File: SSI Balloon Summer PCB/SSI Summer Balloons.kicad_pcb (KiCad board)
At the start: 4 copper layers, 94.5 x 59 mm, 105 parts, among them J1 Battery connector, J2 Conn_01x02, J3 LoRa antenna, J4 APRS antenna, J5 Conn_01x05, J6 1040310811, J7 GPS antenna, J8 PT1000 Sensor, J9 Camera, Q2 DMG2305UX-7, SW2 SW_SPST, SW3 SW_SPST, U1 RFM95W-915S2, U10 MS5611-01BA03, U11 TPS63070RNMR, U12 TPS63070RNMR, U3 AP2112K-3.3TRG1, U4 ICM-42688-P, U5 DRA818V, U7 STM32F411CEUx, U8 MAX-M10S-00B, U9 MAX31865ATP_T, Y1 ABM8W-12.0000MHZ-8-K1Z-T3

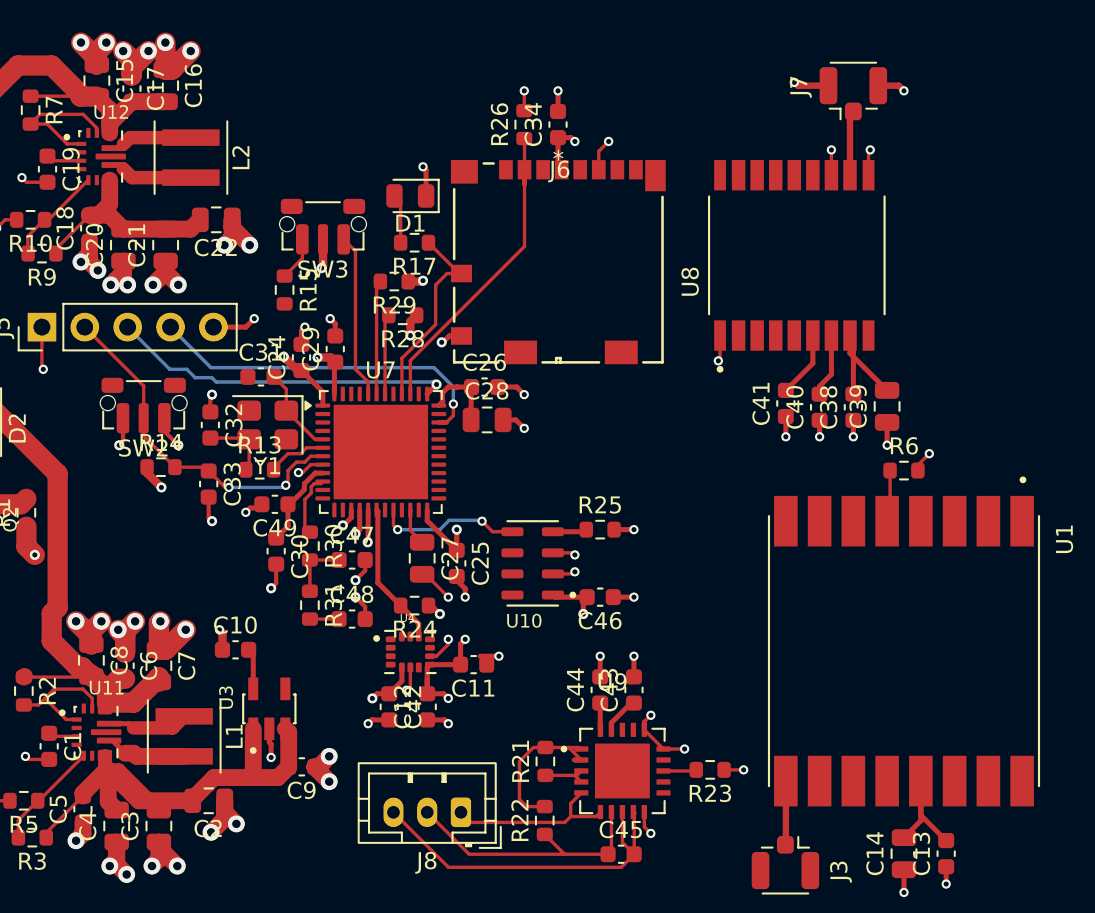
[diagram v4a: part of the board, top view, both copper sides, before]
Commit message: Routed most of SPI
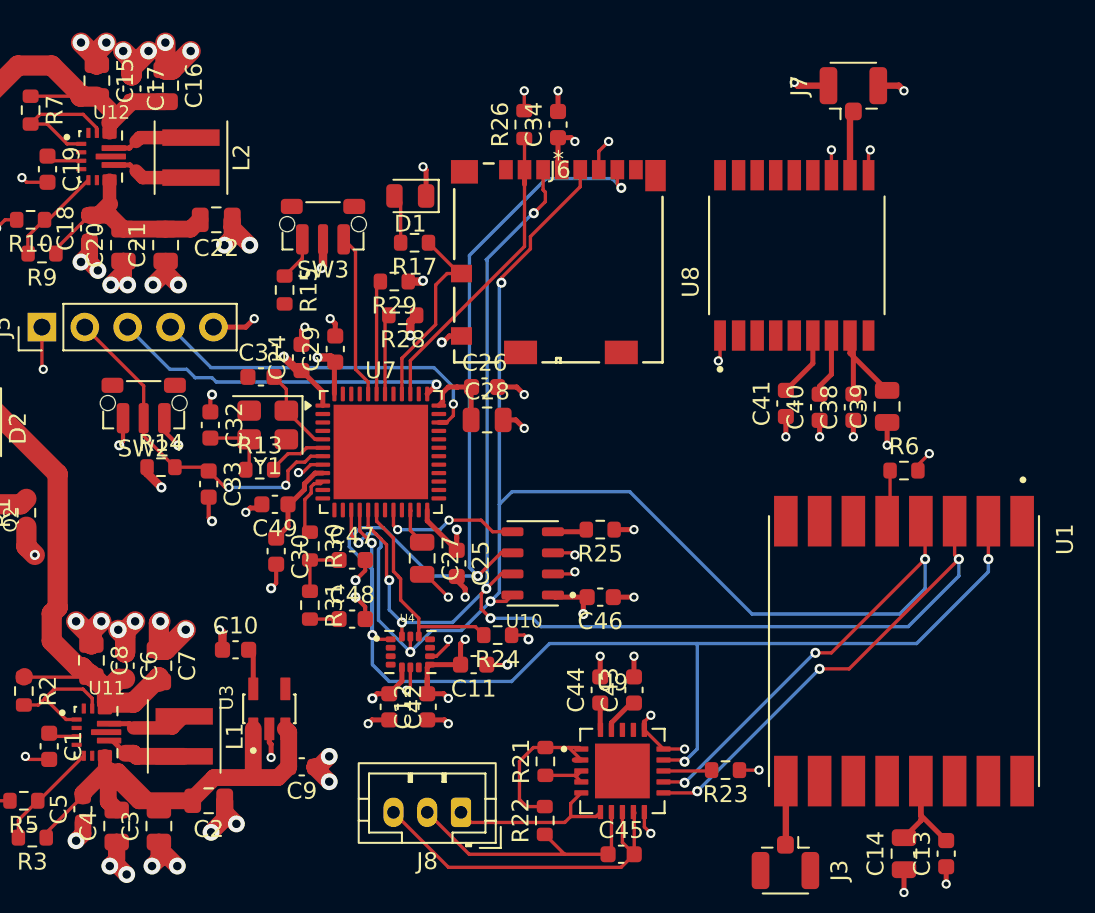
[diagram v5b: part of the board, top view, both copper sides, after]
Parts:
- moved R24 5.23 mm to (139.4, 118.2)
- moved R23 0.91 mm to (152.9, 126.2)
- turned R25 to 180 degrees
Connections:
- R25 pad 1: /MCU (STM)/BARO_CS -> +3V3
- R25 pad 2: +3V3 -> /MCU (STM)/BARO_CS
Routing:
- net /MCU (STM)/MISO: track 1.52 -> 111.4 mm, vias 1 -> 6
- net /MCU (STM)/SCK: track 1.14 -> 101.8 mm, vias 1 -> 7
- net /MCU (STM)/MOSI: track 1.92 -> 100.4 mm, vias 1 -> 8
- net /MCU (STM)/IMU_CS: track 8.53 -> 12.6 mm
- net /MCU (STM)/Temp_CS: track 1.97 -> 2.87 mm
- net VBAT_PROT: track 74.7 -> 73.9 mm
- net Net-(U12-L1): track 4.15 -> 4.83 mm
- net Net-(U12-L2): track 4.21 -> 4.89 mm
